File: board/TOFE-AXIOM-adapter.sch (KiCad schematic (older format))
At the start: 4 parts, among them U1 TOFE-8X

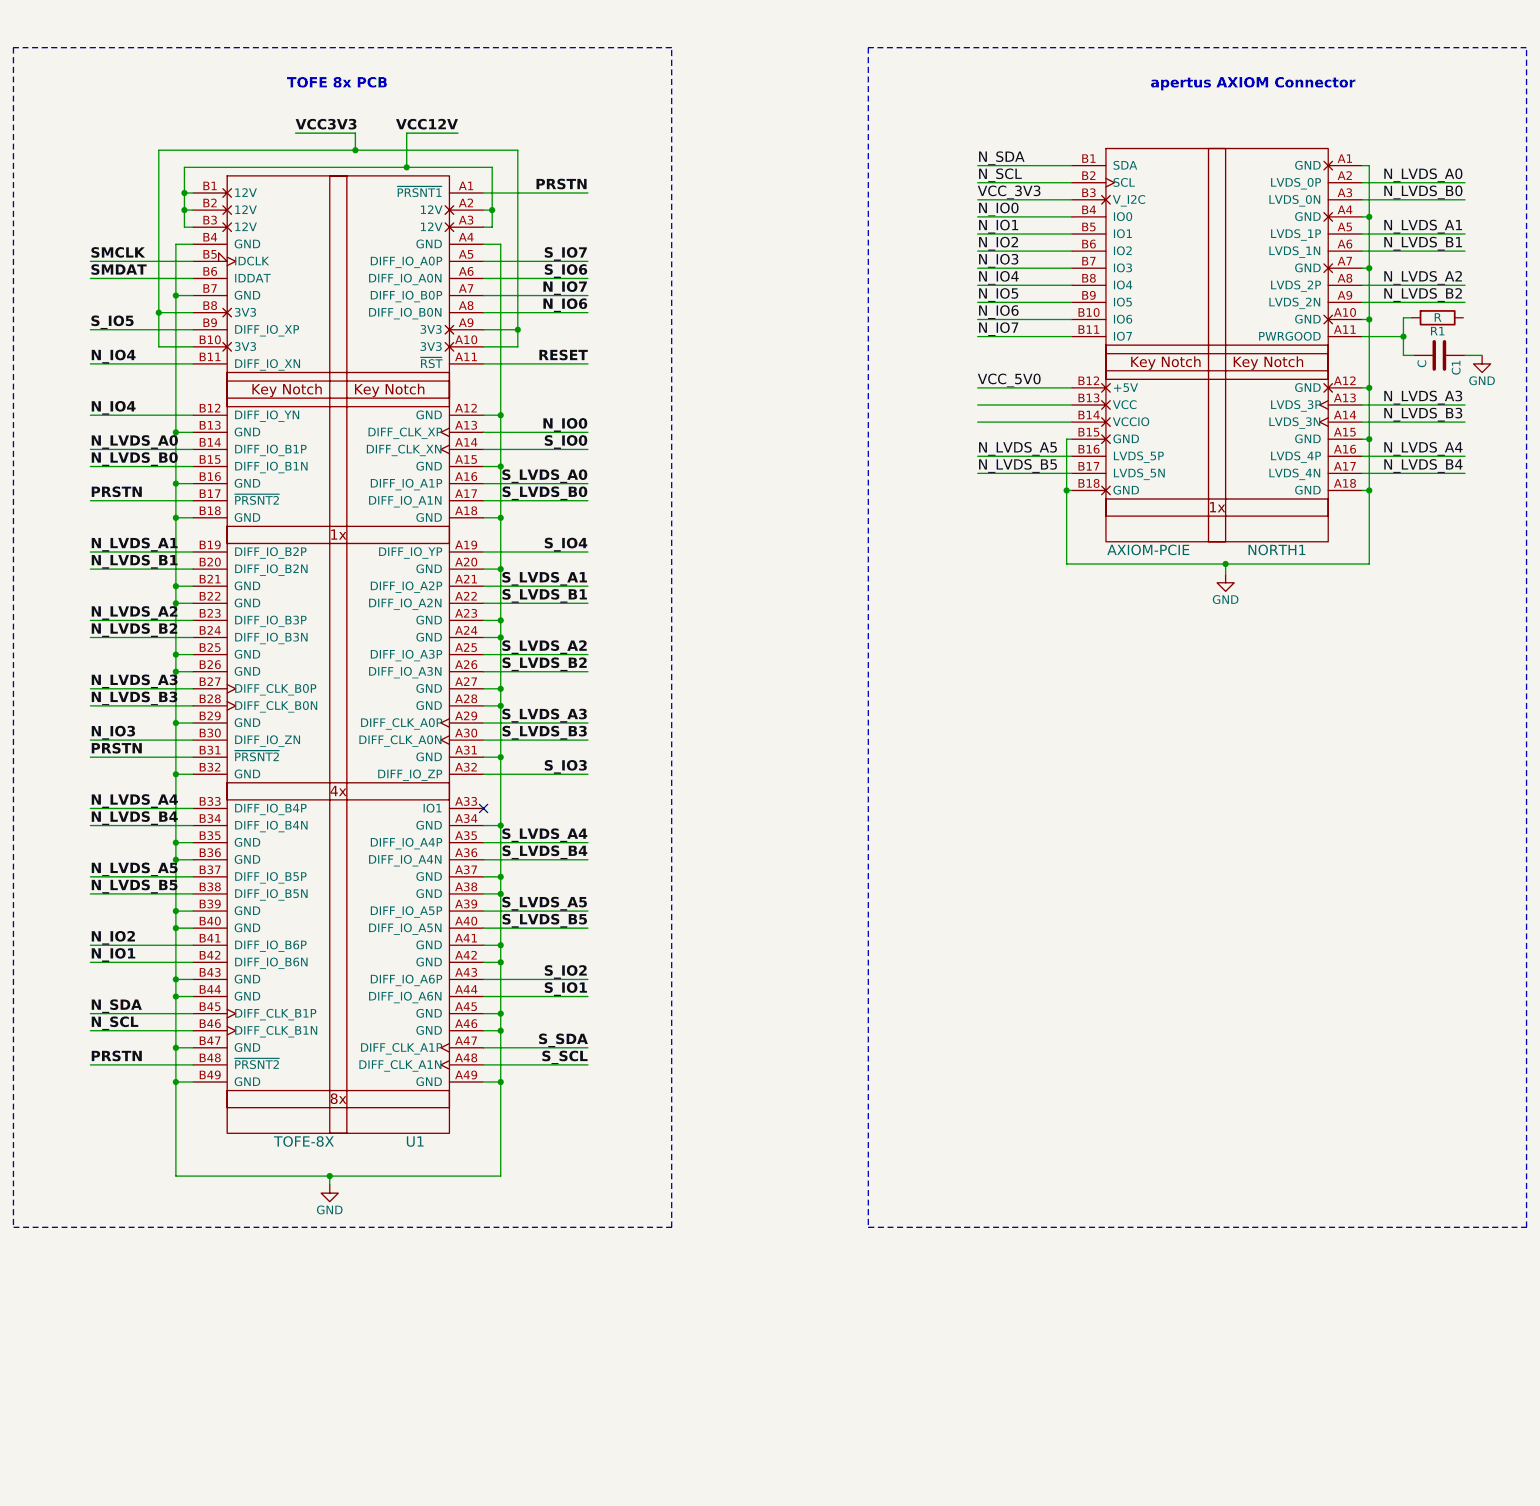
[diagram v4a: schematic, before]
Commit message: Importing the ID EEPROM.
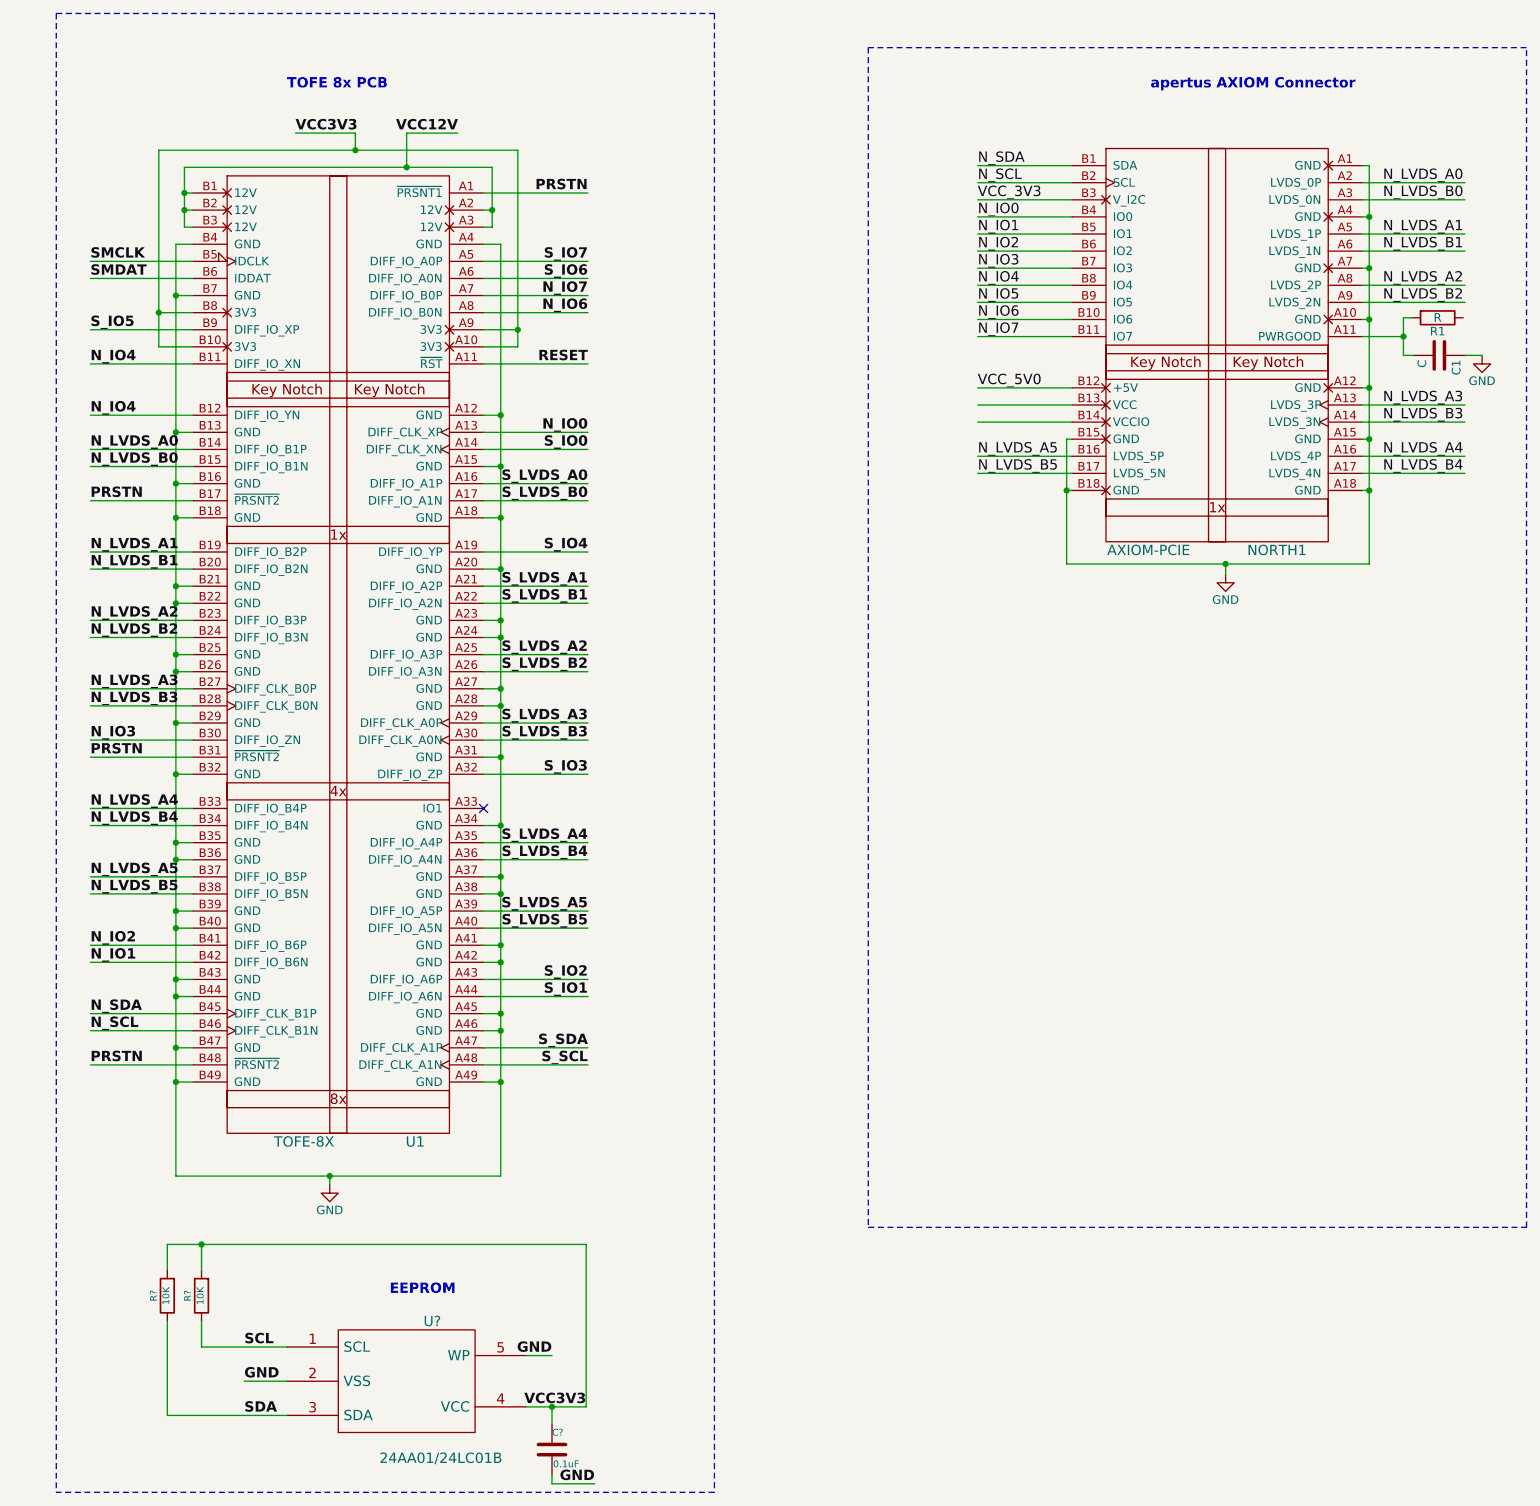
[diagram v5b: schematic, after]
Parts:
- added C?: 0.1uF, ~, symbol C
- added R? (x2): 10K, ~, symbol R
- added U?: 24AA01/24LC01B, ~, symbol 24AA01/24LC01B
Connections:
- net labels added: SCL, SDA
- wire segments 155 -> 171
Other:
- note added: "EEPROM"
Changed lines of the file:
@@
 Wire Wire Line
 	5600 3550 6210 3550
-Wire Notes Line
-	2850 8600 6700 8600
-Wire Notes Line
-	6700 8600 6700 1700
-Wire Notes Line
-	6700 1700 2850 1700
-Wire Notes Line
-	2850 1700 2850 8600
 Wire Wire Line
 	3900 4350 3300 4350
@@
 	1    0    0    -1
 $EndComp
+$Comp
+L 24AA01/24LC01B U?
+U 1 1 56EBC2B6
+P 5150 9500
+F 0 "U?" H 5300 9850 60  0000 C CNN
+F 1 "24AA01/24LC01B" H 5350 9050 60  0000 C CNN
+F 2 "~" H 5150 9500 60  0000 C CNN
+F 3 "~" H 5150 9500 60  0000 C CNN
+	1    5150 9500
+	1    0    0    -1
+$EndComp
+Text Label 6200 9650 2    60   ~ 12
+VCC3V3
+Text Label 4200 9500 0    60   ~ 12
+GND
+Text Label 4200 9300 0    60   ~ 12
+SCL
+Text Label 4200 9700 0    60   ~ 12
+SDA
+Text Notes 5050 9000 0    60   ~ 12
+EEPROM
+$Comp
+L R R?
+U 1 1 56EBC2B7
+P 3950 9000
+F 0 "R?" V 4030 9000 40  0000 C CNN
+F 1 "10K" V 3957 9001 40  0000 C CNN
+F 2 "~" V 3880 9000 30  0000 C CNN
+F 3 "~" H 3950 9000 30  0000 C CNN
+	1    3950 9000
+	-1   0    0    1
+$EndComp
+$Comp
+L R R?
+U 1 1 56EBC2B8
+P 3750 9000
+F 0 "R?" V 3830 9000 40  0000 C CNN
+F 1 "10K" V 3757 9001 40  0000 C CNN
+F 2 "~" V 3680 9000 30  0000 C CNN
+F 3 "~" H 3750 9000 30  0000 C CNN
+	1    3750 9000
+	-1   0    0    1
+$EndComp
+Text Label 6000 9350 2    60   ~ 12
+GND
+$Comp
+L C C?
+U 1 1 56EBC2B9
+P 6000 9900
+F 0 "C?" H 6000 10000 40  0000 L CNN
+F 1 "0.1uF" H 6006 9815 40  0000 L CNN
+F 2 "~" H 6038 9750 30  0000 C CNN
+F 3 "~" H 6000 9900 60  0000 C CNN
+	1    6000 9900
+	1    0    0    -1
+$EndComp
+Text Label 6250 10100 2    60   ~ 12
+GND
+Wire Wire Line
+	5850 9350 6000 9350
+Wire Wire Line
+	3950 9300 4450 9300
+Wire Wire Line
+	3750 9700 4450 9700
+Wire Wire Line
+	4450 9500 4200 9500
+Wire Notes Line
+	3100 1500 3100 10150
+Wire Notes Line
+	3100 1500 6950 1500
+Wire Notes Line
+	6950 1500 6950 10150
+Wire Notes Line
+	6950 10150 3100 10150
+Wire Wire Line
+	5850 9650 6000 9650
+Wire Wire Line
+	6000 9650 6200 9650
+Wire Wire Line
+	3950 9150 3950 9300
+Wire Wire Line
+	3750 9150 3750 9700
+Wire Wire Line
+	3750 8700 3750 8850
+Wire Wire Line
+	3750 8700 3950 8700
+Wire Wire Line
+	3950 8700 6200 8700
+Wire Wire Line
+	3950 8700 3950 8850
+Connection ~ 3950 8700
+Wire Wire Line
+	6200 8700 6200 9650
+Wire Wire Line
+	6000 9650 6000 9750
+Connection ~ 6000 9650
+Wire Wire Line
+	6000 10100 6250 10100
+Wire Wire Line
+	6000 10050 6000 10100
 $EndSCHEMATC

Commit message: Associating footprints.
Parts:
- C1: renamed from C?; footprint ~ -> (none)
- R1, R2: renamed from R?; footprint ~ -> Resistors_SMD:R_0603_HandSoldering
- U1: renamed from U?; footprint ~ -> (none)
- renumbered C1 to CN1, R1 to RN1, U1 to TOFE1
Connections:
- wire segments 171 -> 169
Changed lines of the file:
@@
 LIBS:TOFE
 LIBS:axiom
+LIBS:EEPROM
 EELAYER 25 0
 EELAYER END
@@
 PRSTN
 $Comp
-L TOFE-8X U1
+L TOFE-8X TOFE1
 U 1 1 560CFB49
 P 5200 5250
-F 0 "U1" H 5200 2400 60  0000 C CNN
+F 0 "TOFE1" H 5200 2400 60  0000 C CNN
 F 1 "TOFE-8X" H 4550 2400 60  0000 C CNN
 F 2 "TOFE_8X_HalfHeight:TOFE_8X_HalfHeight" H 3900 4950 60  0001 C CNN
@@
 	10740 3390 10980 3390
 $Comp
-L R R1
+L R RN1
 U 1 1 56EBC757
 P 11180 3280
-F 0 "R1" V 11260 3280 50  0000 C CNN
+F 0 "RN1" V 11260 3280 50  0000 C CNN
 F 1 "R" V 11180 3280 50  0000 C CNN
 F 2 "Resistors_SMD:R_0603_HandSoldering" V 11110 3280 50  0001 C CNN
@@
 $EndComp
 $Comp
-L C C1
+L C CN1
 U 1 1 56EBC822
 P 11190 3500
-F 0 "C1" H 11215 3600 50  0000 L CNN
+F 0 "CN1" H 11215 3600 50  0000 L CNN
 F 1 "C" H 11215 3400 50  0000 L CNN
 F 2 "Capacitors_SMD:C_1206_HandSoldering" H 11228 3350 50  0001 C CNN
@@
 $EndComp
 $Comp
-L 24AA01/24LC01B U?
+L 24AA01/24LC01B U1
 U 1 1 56EBC2B6
 P 5150 9500
-F 0 "U?" H 5300 9850 60  0000 C CNN
+F 0 "U1" H 5300 9850 60  0000 C CNN
 F 1 "24AA01/24LC01B" H 5350 9050 60  0000 C CNN
-F 2 "~" H 5150 9500 60  0000 C CNN
+F 2 "" H 5150 9500 60  0001 C CNN
 F 3 "~" H 5150 9500 60  0000 C CNN
 	1    5150 9500
@@
 EEPROM
 $Comp
-L R R?
+L R R2
 U 1 1 56EBC2B7
 P 3950 9000
-F 0 "R?" V 4030 9000 40  0000 C CNN
+F 0 "R2" V 4030 9000 40  0000 C CNN
 F 1 "10K" V 3957 9001 40  0000 C CNN
-F 2 "~" V 3880 9000 30  0000 C CNN
+F 2 "Resistors_SMD:R_0603_HandSoldering" V 3880 9000 30  0000 C CNN
 F 3 "~" H 3950 9000 30  0000 C CNN
 	1    3950 9000
@@
 $EndComp
 $Comp
-L R R?
+L R R1
 U 1 1 56EBC2B8
 P 3750 9000
-F 0 "R?" V 3830 9000 40  0000 C CNN
+F 0 "R1" V 3830 9000 40  0000 C CNN
 F 1 "10K" V 3757 9001 40  0000 C CNN
-F 2 "~" V 3680 9000 30  0000 C CNN
+F 2 "Resistors_SMD:R_0603_HandSoldering" V 3680 9000 30  0000 C CNN
 F 3 "~" H 3750 9000 30  0000 C CNN
 	1    3750 9000
 	-1   0    0    1
 $EndComp
-Text Label 6000 9350 2    60   ~ 12
-GND
-$Comp
-L C C?
+$Comp
+L C C1
 U 1 1 56EBC2B9
 P 6000 9900
-F 0 "C?" H 6000 10000 40  0000 L CNN
+F 0 "C1" H 6000 10000 40  0000 L CNN
 F 1 "0.1uF" H 6006 9815 40  0000 L CNN
-F 2 "~" H 6038 9750 30  0000 C CNN
+F 2 "" H 6038 9750 30  0001 C CNN
 F 3 "~" H 6000 9900 60  0000 C CNN
 	1    6000 9900
@@
 	6950 10150 3100 10150
 Wire Wire Line
-	5850 9650 6000 9650
-Wire Wire Line
-	6000 9650 6200 9650
+	5850 9650 6200 9650
 Wire Wire Line
 	3950 9150 3950 9300
@@
 	3750 8700 3750 8850
 Wire Wire Line
-	3750 8700 3950 8700
-Wire Wire Line
-	3950 8700 6200 8700
+	3750 8700 6200 8700
 Wire Wire Line
 	3950 8700 3950 8850
@@
 Wire Wire Line
 	6000 10050 6000 10100
+$Comp
+L GND #PWR?
+U 1 1 56EBC6DB
+P 6000 9350
+F 0 "#PWR?" H 6000 9100 50  0001 C CNN
+F 1 "GND" H 6000 9200 50  0000 C CNN
+F 2 "" H 6000 9350 50  0000 C CNN
+F 3 "" H 6000 9350 50  0000 C CNN
+	1    6000 9350
+	1    0    0    -1
+$EndComp
 $EndSCHEMATC
